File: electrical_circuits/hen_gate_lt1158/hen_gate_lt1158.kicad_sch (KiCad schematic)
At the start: 13 parts, among them IC1 LT1158ISW, Q1 IRF540ZPBF, Q2 IRF540ZPBF

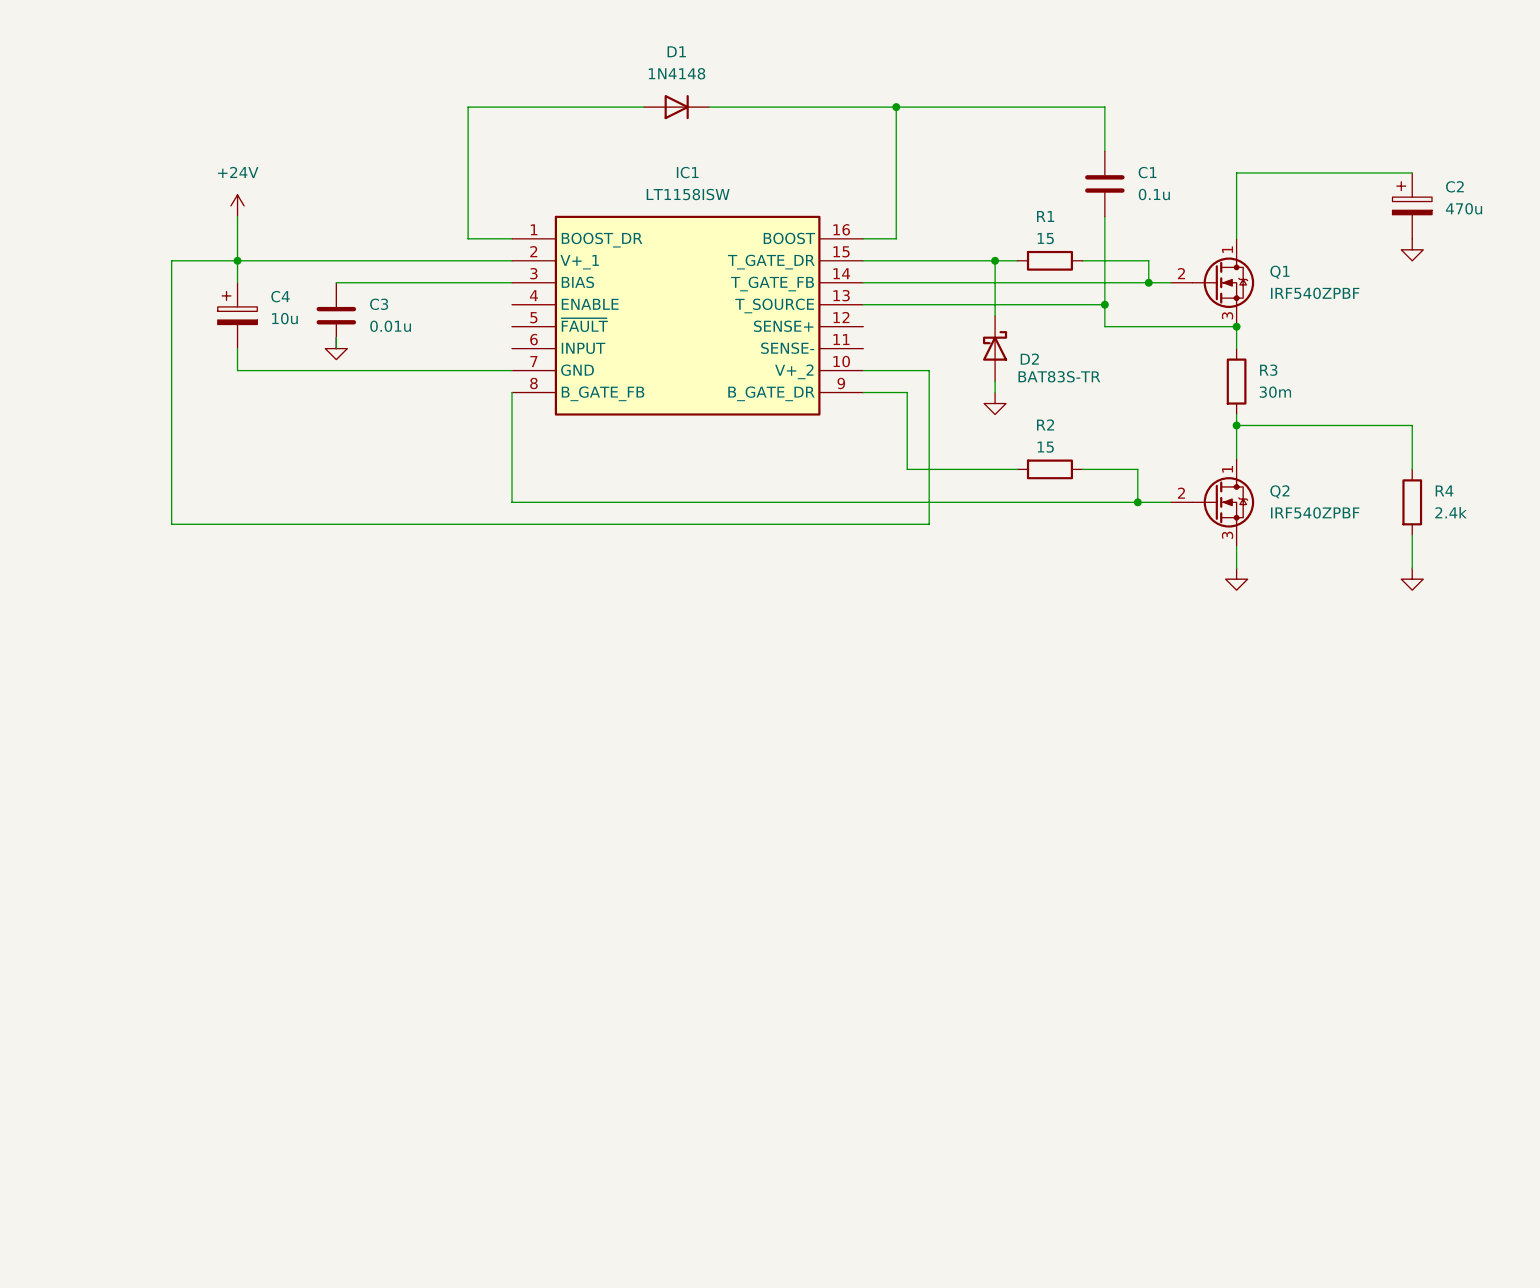
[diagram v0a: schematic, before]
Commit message: Introduced new IC - IFX007T half bridge (INFINEON). Begin power scheme.
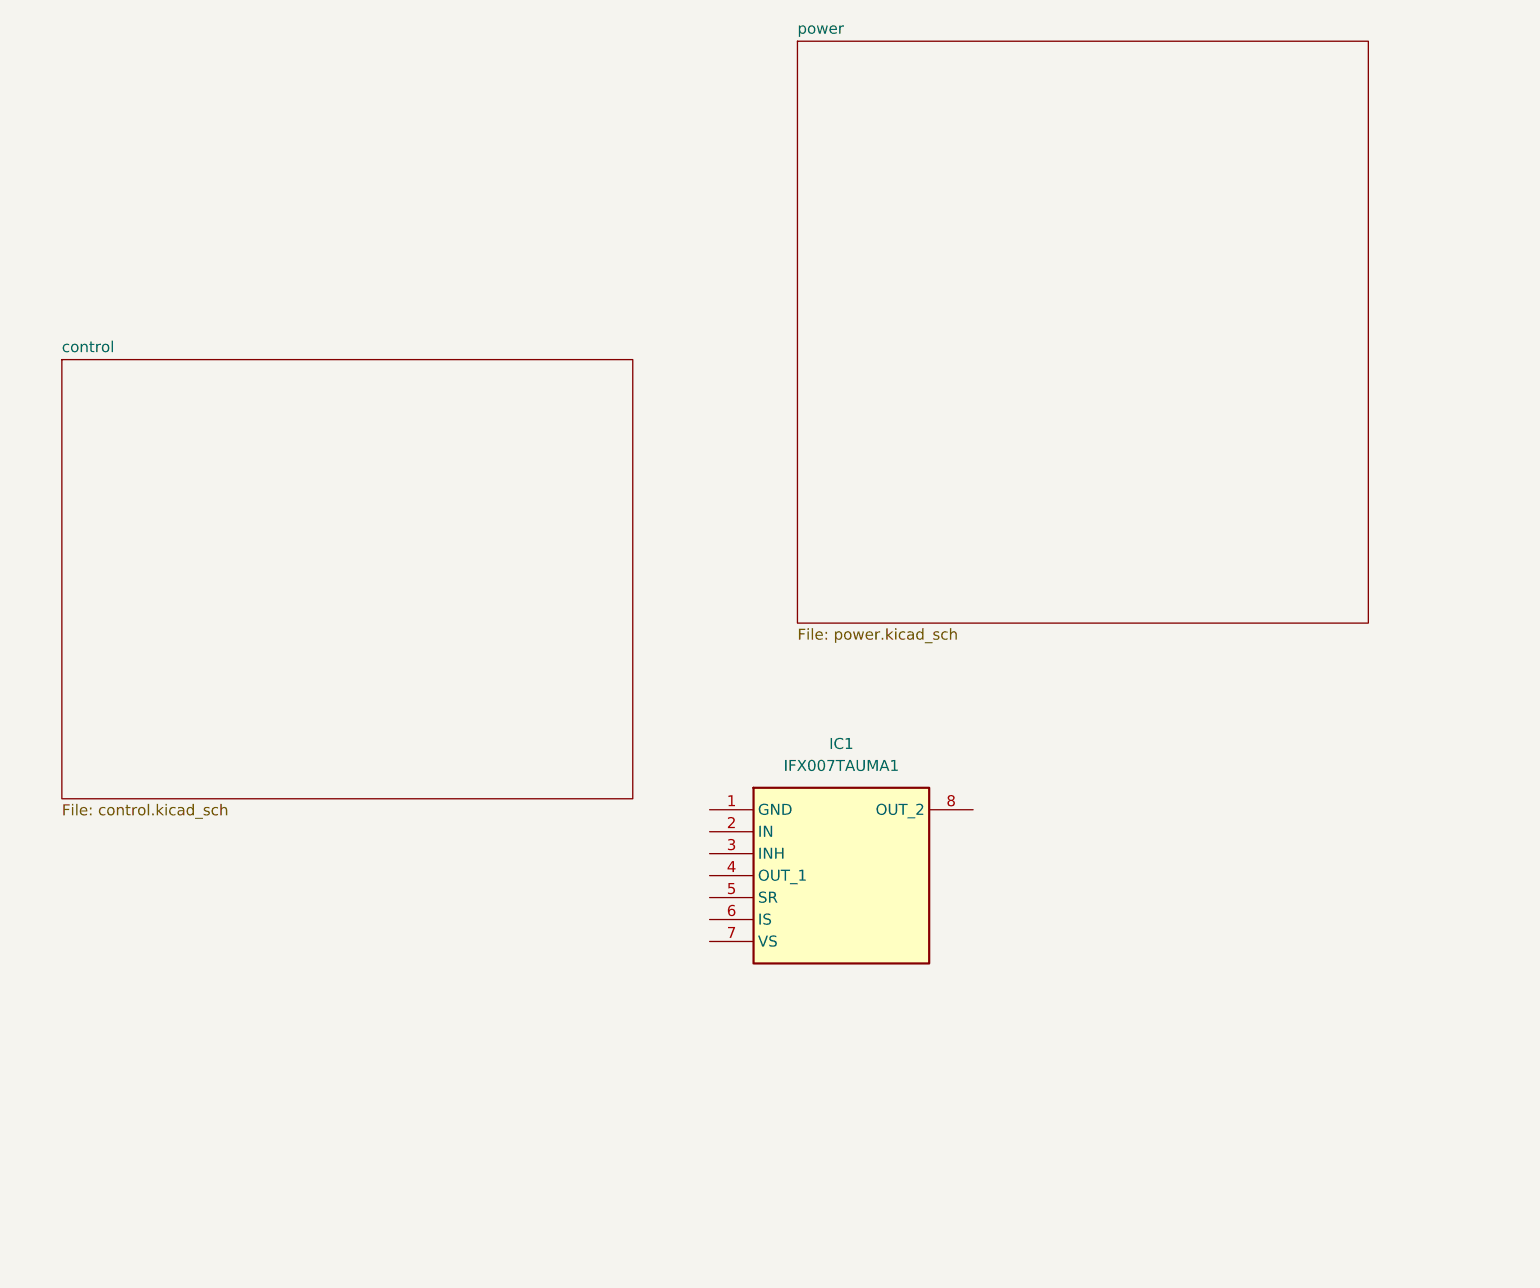
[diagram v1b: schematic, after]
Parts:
- removed C1: 0.1u, Capacitor_SMD:C_0805_2012Metric, symbol Device:C
- removed C2: 470u, Capacitor_THT:CP_Radial_D12.5mm_P2.50mm, symbol Device:C_Polarized
- removed C3: 0.01u, Capacitor_SMD:C_0805_2012Metric, symbol Device:C
- removed C4: 10u, symbol Device:C_Polarized
- removed D1: 1N4148, Diode_SMD:D_SOD-123, symbol Device:D
- removed D2: BAT83S-TR, Diode_THT:D_DO-35_SOD27_P7.62mm_Horizontal, symbol Device:D_Schottky
- removed IC1: LT1158ISW, SOIC127P1032X264-16N, symbol LT1158ISW:LT1158ISW#PBF
- removed Q1, Q2: IRF540ZPBF, Package_TO_SOT_THT:TO-220-3_Vertical, symbol Device:Q_NMOS_DGS
- removed R1, R2: 15, Resistor_SMD:R_0805_2012Metric_Pad1.20x1.40mm_HandSolder, symbol Device:R
- removed R3: 30m, CSSH2728:RESC6771X124N, symbol Device:R
- removed R4: 2.4k, symbol Device:R
- added IC1: IFX007TAUMA1, PG-TO263-7-1, symbol IFX007TAUMA1:IFX007TAUMA1
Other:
- added sheet control (control.kicad_sch)
- added sheet power (power.kicad_sch)

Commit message: Added 8-bit uC to hen_gate_lt1158 project.
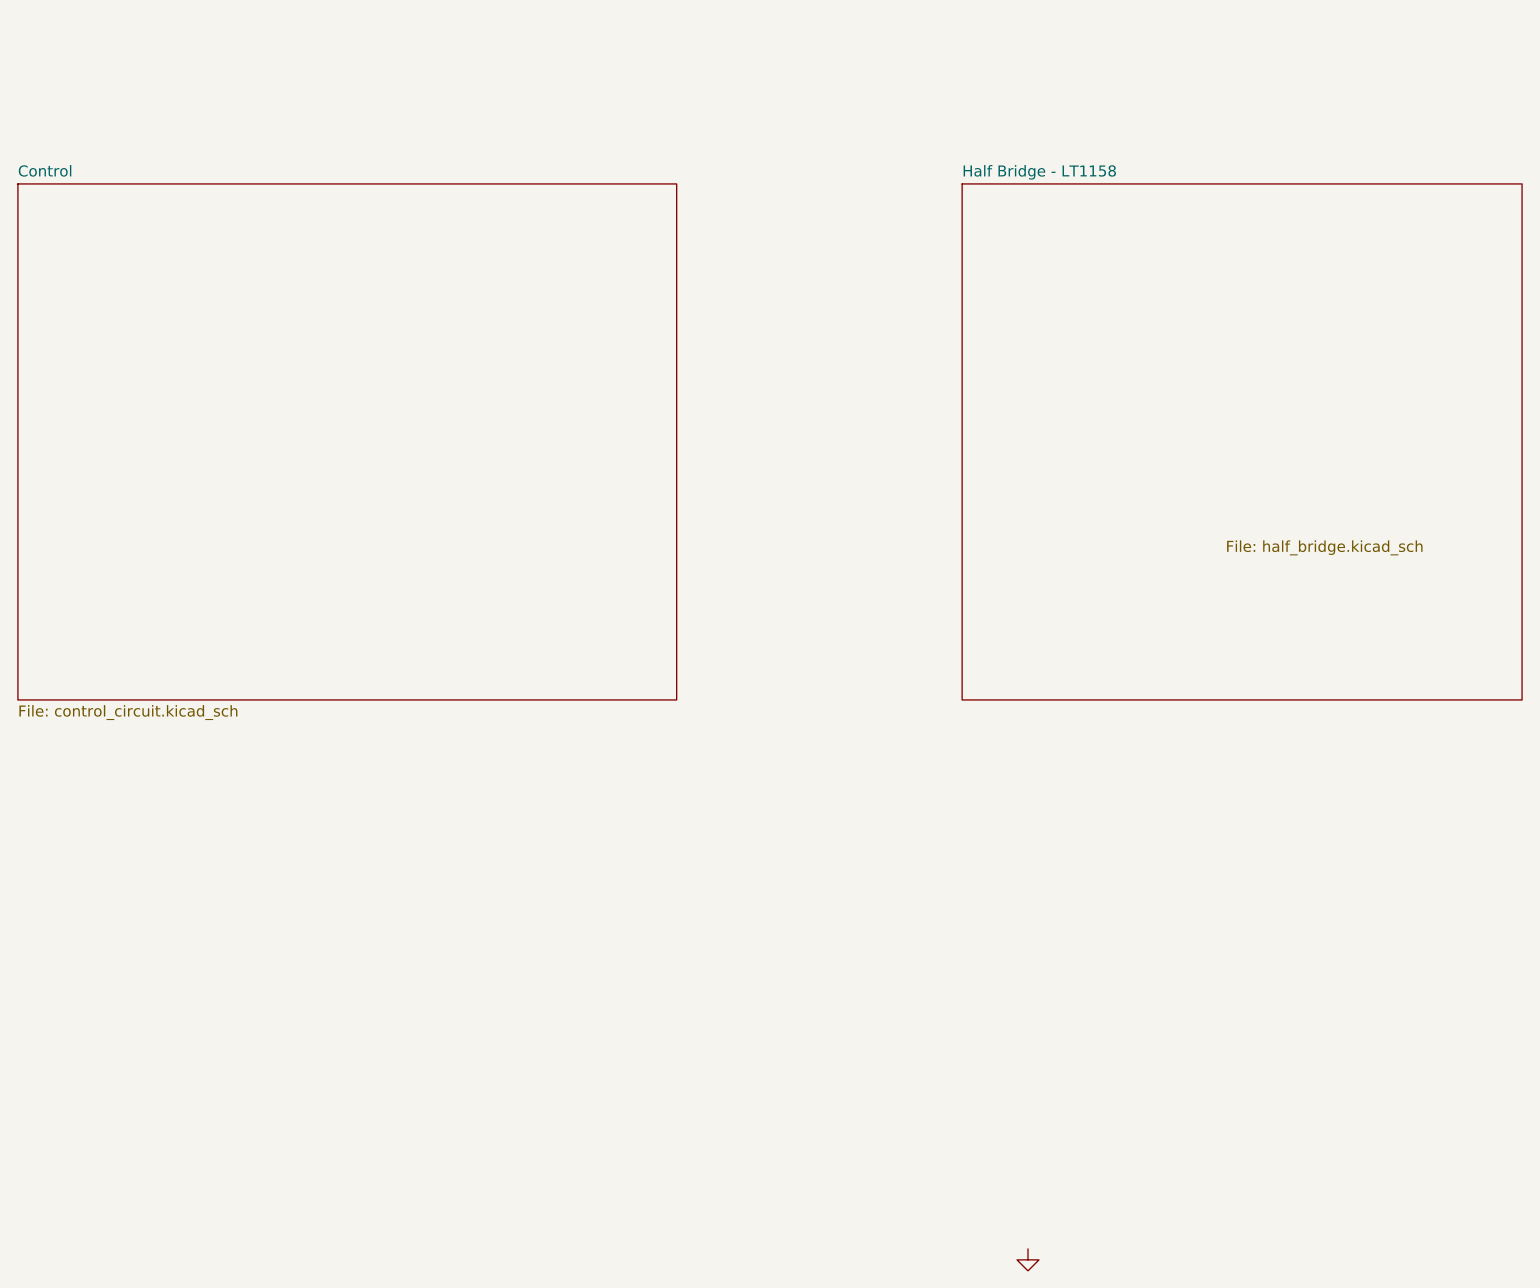
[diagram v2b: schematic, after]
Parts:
- removed IC1: IFX007TAUMA1, PG-TO263-7-1, symbol IFX007TAUMA1:IFX007TAUMA1
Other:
- removed sheet control
- removed sheet power
- added sheet Control (control_circuit.kicad_sch)
- added sheet Half Bridge - LT1158 (half_bridge.kicad_sch)
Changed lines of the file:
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@@
 	(paper "A4")
 	(symbol
-		(lib_id "IFX007TAUMA1:IFX007TAUMA1")
-		(at 143.51 132.08 0)
+		(lib_id "power:GND")
+		(at 180.34 182.88 0)
 		(unit 1)
 		(exclude_from_sim no)
@@
 		(dnp no)
 		(fields_autoplaced yes)
-		(property "Reference" "IC1"
-			(at 158.75 124.46 0)
-			(effects
-				(font
-					(size 1.27 1.27)
-				)
-			)
-		)
-		(property "Value" "IFX007TAUMA1"
-			(at 158.75 127 0)
-			(effects
-				(font
-					(size 1.27 1.27)
-				)
-			)
-		)
-		(property "Footprint" "PG-TO263-7-1"
-			(at 170.18 227 0)
-			(effects
-				(font
-					(size 1.27 1.27)
-				)
-				(justify left top)
-				(hide yes)
-			)
-		)
-		(property "Datasheet" "https://www.infineon.com/dgdl/Infineon-IFX007T-DS-v01_00-EN.pdf?fileId=5546d46265f064ff0166433484070b75"
-			(at 170.18 327 0)
-			(effects
-				(font
-					(size 1.27 1.27)
-				)
-				(justify left top)
-				(hide yes)
-			)
-		)
-		(property "Description" "Gate Drivers"
-			(at 143.51 132.08 0)
+		(property "Reference" "#PWR3"
+			(at 180.34 189.23 0)
 			(effects
 				(font
@@
 			)
 		)
-		(property "Height" ""
-			(at 170.18 527 0)
+		(property "Value" "GND"
+			(at 180.34 187.96 0)
 			(effects
 				(font
 					(size 1.27 1.27)
 				)
-				(justify left top)
 				(hide yes)
 			)
 		)
-		(property "Mouser Part Number" "726-IFX007TAUMA1"
-			(at 170.18 627 0)
+		(property "Footprint" ""
+			(at 180.34 182.88 0)
 			(effects
 				(font
 					(size 1.27 1.27)
 				)
-				(justify left top)
 				(hide yes)
 			)
 		)
-		(property "Mouser Price/Stock" "https://www.mouser.co.uk/ProductDetail/Infineon-Technologies/IFX007TAUMA1?qs=qSfuJ%252Bfl%2Fd7ZcDPqNlCgmA%3D%3D"
-			(at 170.18 727 0)
+		(property "Datasheet" ""
+			(at 180.34 182.88 0)
 			(effects
 				(font
 					(size 1.27 1.27)
 				)
-				(justify left top)
 				(hide yes)
 			)
 		)
-		(property "Manufacturer_Name" "Infineon"
-			(at 170.18 827 0)
+		(property "Description" "Power symbol creates a global label with name \"GND\" , ground"
+			(at 180.34 182.88 0)
 			(effects
 				(font
 					(size 1.27 1.27)
 				)
-				(justify left top)
 				(hide yes)
 			)
 		)
-		(property "Manufacturer_Part_Number" "IFX007TAUMA1"
-			(at 170.18 927 0)
-			(effects
-				(font
-					(size 1.27 1.27)
-				)
-				(justify left top)
-				(hide yes)
-			)
-		)
-		(pin "7"
-		)
-		(pin "5"
-		)
-		(pin "6"
-		)
-		(pin "4"
-		)
 		(pin "1"
 		)
-		(pin "3"
-		)
-		(pin "2"
-		)
-		(pin "8"
-		)
 		(instances
-			(project ""
+			(project "hen_gate_lt1158"
 				(path "/a762bba9-2ae1-4991-be5c-6810d4bd1a2c"
-					(reference "IC1")
+					(reference "#PWR3")
 					(unit 1)
 				)
@@
 	)
 	(sheet
-		(at 68.58 80.01)
-		(size 66.04 50.8)
+		(at 63.5 59.69)
+		(size 76.2 59.69)
 		(fields_autoplaced yes)
 		(stroke
@@
 			(color 0 0 0 0.0000)
 		)
-		(property "Sheetname" "control"
-			(at 68.58 79.2984 0)
+		(property "Sheetname" "Control"
+			(at 63.5 58.9784 0)
 			(effects
 				(font
@@
 			)
 		)
-		(property "Sheetfile" "control.kicad_sch"
-			(at 68.58 131.3946 0)
+		(property "Sheetfile" "control_circuit.kicad_sch"
+			(at 63.5 119.9646 0)
 			(effects
 				(font
@@
 	)
 	(sheet
-		(at 153.67 43.18)
-		(size 66.04 67.31)
-		(fields_autoplaced yes)
+		(at 172.72 59.69)
+		(size 64.77 59.69)
 		(stroke
 			(width 0.1524)
@@
 			(color 0 0 0 0.0000)
 		)
-		(property "Sheetname" "power"
-			(at 153.67 42.4684 0)
+		(property "Sheetname" "Half Bridge - LT1158"
+			(at 172.72 58.9784 0)
 			(effects
 				(font
@@
 			)
 		)
-		(property "Sheetfile" "power.kicad_sch"
-			(at 153.67 111.0746 0)
+		(property "Sheetfile" "half_bridge.kicad_sch"
+			(at 203.2 100.9146 0)
 			(effects
 				(font
